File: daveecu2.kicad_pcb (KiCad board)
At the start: 4 copper layers, 160 x 117.5 mm, 242 parts, among them J1 CONN_BLACK, J2 CONN_GREY, J3 SWD, J4 USB_B, J5 USB_EXT, J6 Micro_SD_Card_Det, J7 HC-05, Q1 AO3401A, Q2 2N7002, Q3 2N7002, Q4 2N7002, U1 MPXH6250A, U10 USBLC6-2SC6, U11 MCP2551-I-SN, U12 STM32F429ZGTx, U13 VNLD5090, U14 VNLD5090, U16 ATECC608A-SSHDA, U2 VNLD5090, U3 VNLD5090, U4 TC4424A, U5 TC4424A, U6 SP720, U7 VNLD5090, U8 TPS5430DDA, U9 TPS5430DDA, Y1 25mhz, Y2 Crystal

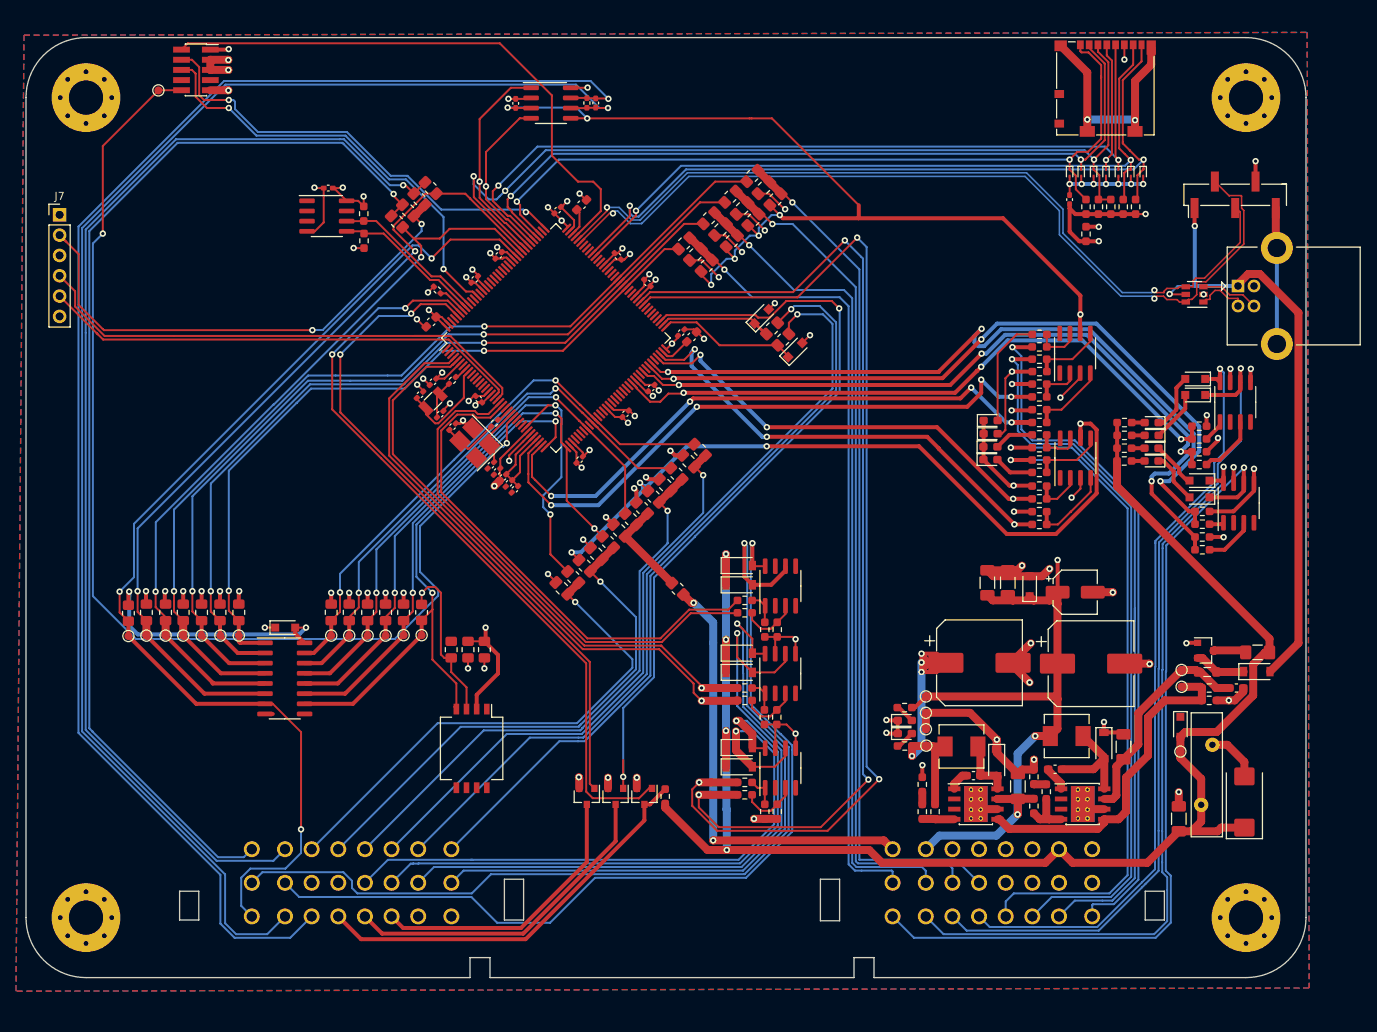
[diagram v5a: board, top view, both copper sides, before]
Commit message: Schematic and Layout Updates
* cleanup unused pins for DRC
* swap swd connector for the fancy one the phill uses
* swap out the CAN transciever for one more suitable for 3v3
* reroute CAN differential pair
* clean up copper pours
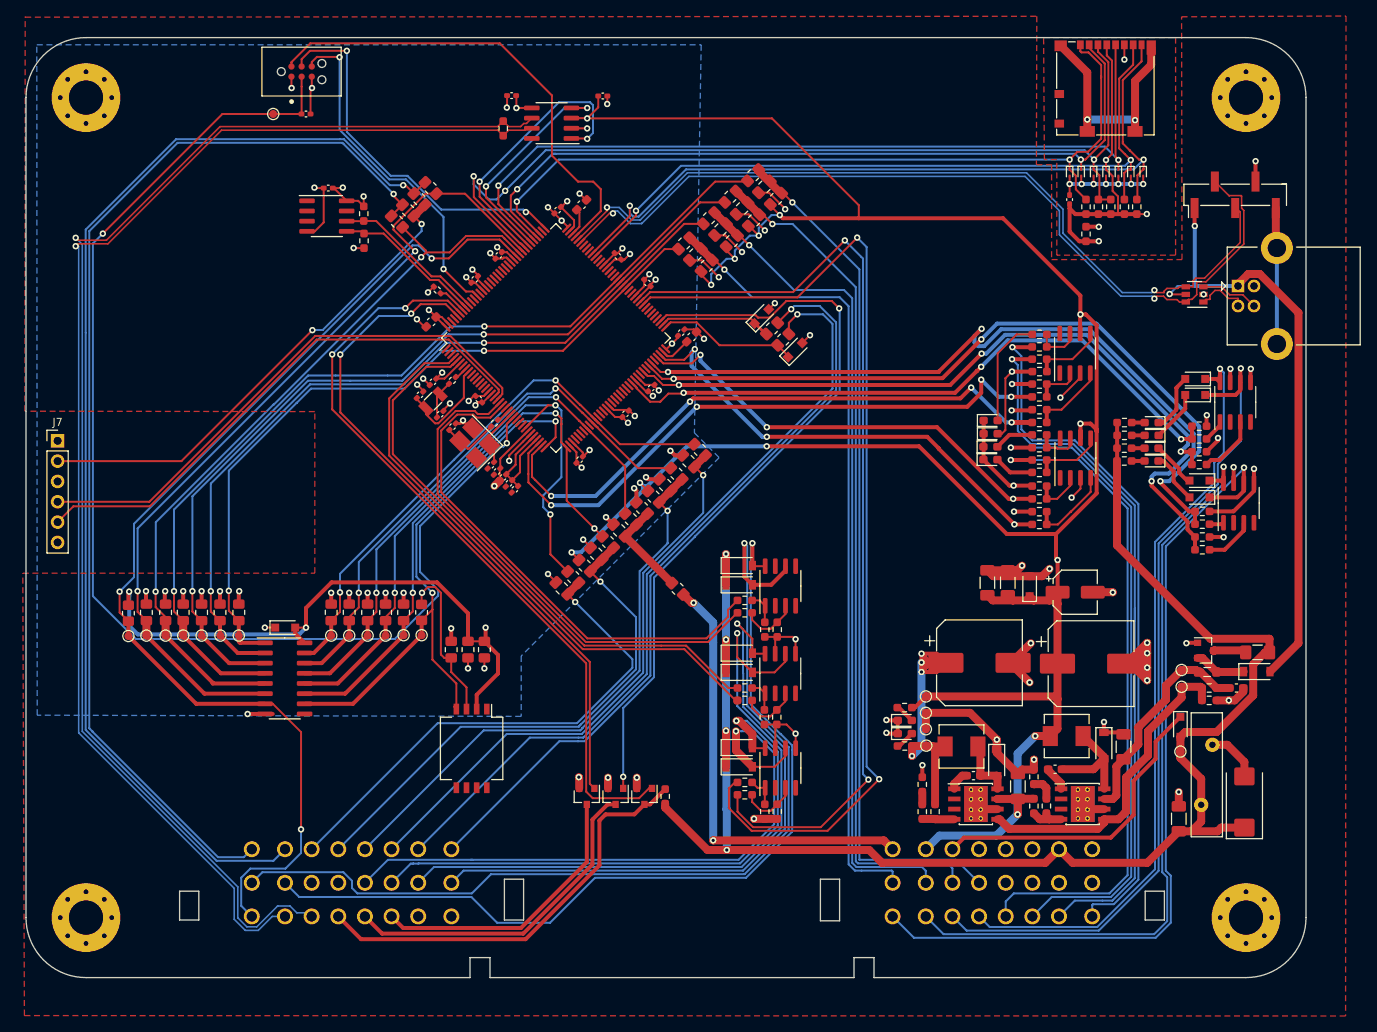
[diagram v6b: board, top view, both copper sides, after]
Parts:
- added C61: 100n, Capacitor_SMD:C_0402_1005Metric_Pad0.74x0.62mm_HandSolder, F.Cu at (87.1, 29.8)
- C23: value 0.1u -> 100n
- C24: value 100p -> 100n
- J3: footprint Connector_PinSocket_1.27mm:PinSocket_2x05_P1.27mm_Vertical_SMD -> TC2030-IDC-NL:TAG_TC2030-IDC-NL
- R58: value 60 -> 120; footprint Resistor_SMD:R_0402_1005Metric_Pad0.72x0.64mm_HandSolder -> Resistor_SMD:R_0603_1608Metric_Pad0.98x0.95mm_HandSolder
- U11: value MCP2551-I-SN -> TJA1051T-3
- moved J7 28.3 mm to (18.9, 72.9)
- moved C23 26.2 mm to (50.0, 32.0), turned to 0 degrees
- moved TP9 14.7 mm to (45.9, 32.0)
- moved J3 13.2 mm to (49.5, 26.8)
- moved R58 10.9 mm to (74.7, 33.9), turned to 270 degrees
- moved C24 10.6 mm to (75.7, 29.8), turned to 0 degrees
- moved U11 2.52 mm to (80.7, 33.2), turned to 180 degrees
- moved R56 1.80 mm to (142.6, 118.5)
- moved R76 0.15 mm to (152.3, 43.6)
- moved R77 0.15 mm to (153.8, 43.6)
- moved R10 0.14 mm to (105.9, 39.7)
- moved C46 0.14 mm to (107.3, 41.1)
- moved R2 0.11 mm to (106.0, 45.4)
- moved R4 0.10 mm to (108.8, 42.6)
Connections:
- C23 pad 1: VPROT -> NRST
- C24 pad 1: CANH -> GND
- C24 pad 2: CANL -> +3V3
- D35 pad 1: (no net) -> VREG
- J1 pad A1: (no net) -> GND
- J1 pad A6: GND -> VREG
- J2 pad C6: CANH -> CAN-
- J2 pad C7: CANL -> CAN+
- J3 pad 3: GND -> NRST
- R58 pad 1: CANL -> CAN-
- R58 pad 2: CANH -> CAN+
- U11 pad 5: VPROT -> +3V3
- U11 pad 6: CANL -> CAN-
- U11 pad 7: CANH -> CAN+
- U11 pad 8: GND -> (no net)
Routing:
- net CANH: track 187.2 -> 0.00 mm, vias 1 -> 0
- net CANL: track 182.4 -> 0.00 mm, vias 1 -> 0
- net CAN-: track 0.00 -> 168.7 mm, vias 0 -> 1
- net CAN+: track 0.00 -> 163.9 mm, vias 0 -> 1
- net VREG: track 0.00 -> 39.1 mm
- net VPROT: track 419.6 -> 455.0 mm, vias 19 -> 18
- net GND: track 290.5 -> 306.5 mm, vias 93 -> 97
- net SWDIO: track 71.9 -> 59.4 mm
- net NRST: track 145.7 -> 157.7 mm
- net SWO: track 54.2 -> 43.0 mm
- net SWCLK: track 56.8 -> 46.9 mm
- net /mcu/MCU-PWM1: track 128.5 -> 119.1 mm, vias 3 -> 2
- net MCU-CAN-TX: track 26.4 -> 35.4 mm, vias 1 -> 2
- net /mcu/MCU-VVT: track 134.5 -> 125.6 mm, vias 3 -> 2
- net UART7_RX: track 61.1 -> 68.3 mm
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- added copper zone on In2.Cu, net GND
- added copper zone on F.Cu, net SDIO_VDD
- added copper zone on B.Cu, net VPROT
- removed copper zone on B.Cu, net GND
- removed copper zone on In1.Cu, net GND
- removed copper zone on In1.Cu, net SDIO_VDD
- removed copper zone on In1.Cu, net VPROT

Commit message: More routing updates
* added stitching vias
* organized sensor sheet
* moved the CAN and Security chips closer together to clean up fills
* added silkscreen text to some things
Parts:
- added C62: 0.1uf, Capacitor_SMD:C_0805_2012Metric_Pad1.18x1.45mm_HandSolder, F.Cu at (78.0, 100.7)
- added C63: 1uf, Capacitor_SMD:C_0805_2012Metric_Pad1.18x1.45mm_HandSolder, F.Cu at (80.0, 100.7)
- added C64: 470pf, Capacitor_SMD:C_0805_2012Metric_Pad1.18x1.45mm_HandSolder, F.Cu at (75.9, 100.7)
- added R89: 470, Resistor_SMD:R_0805_2012Metric_Pad1.20x1.40mm_HandSolder, F.Cu at (66.7, 94.3)
- added TP1: TP_BARO, TestPoint:TestPoint_Pad_D1.0mm, F.Cu at (66.7, 97.2)
- added U15: MPXH6250A, Sensor_Pressure:Freescale_98ARH99066A, F.Cu at (79.3, 111.3)
- moved C61 36.0 mm to (56.5, 48.9)
- moved C24 35.1 mm to (45.5, 47.6)
- moved R58 34.4 mm to (44.4, 50.1)
- moved U11 34.4 mm to (50.4, 49.5)
- moved R50 14.5 mm to (45.9, 38.9), turned to 90 degrees
- moved R51 11.5 mm to (46.0, 42.3), turned to 270 degrees
- moved C54 9.22 mm to (43.9, 43.8), turned to 270 degrees
- moved TP9 3.98 mm to (49.4, 34.0)
- moved U16 3.46 mm to (50.6, 42.0), turned to 180 degrees
- moved C45 2.26 mm to (71.8, 100.7)
- moved C47 2.26 mm to (69.7, 100.7)
- moved C9 2.26 mm to (73.8, 100.7)
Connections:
- U6 pad 9: (no net) -> ADC-CLAMP-8
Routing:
- net VPROT: track 455.0 -> 414.5 mm, vias 18 -> 21
- net ADC-CLAMP-8: track 0.00 -> 40.0 mm, vias 0 -> 2
- net CAN-: track 168.7 -> 135.5 mm
- net CAN+: track 163.9 -> 130.7 mm
- net Net-(C64-Pad2): track 0.00 -> 23.8 mm, vias 0 -> 2
- net I2C1_SDA: track 19.6 -> 39.3 mm, vias 0 -> 2
- net I2C1_SDL: track 19.6 -> 36.2 mm, vias 0 -> 2
- net MCU-CAN-RX: track 28.0 -> 36.8 mm, vias 2 -> 1
- net ADC-CLAMP-9: track 74.1 -> 81.4 mm, vias 2 -> 3
- net MCU-CAN-TX: track 35.4 -> 41.7 mm, vias 2 -> 3
- net SWDIO: track 59.4 -> 55.9 mm, vias 0 -> 2
- net NRST: track 157.7 -> 155.1 mm, vias 2 -> 4
- net Net-(C47-Pad2): track 20.8 -> 18.4 mm, vias 1 -> 2
- net +3V3: track 111.8 -> 109.9 mm, vias 25 -> 24
- net GND: track 306.5 -> 306.9 mm, vias 97 -> 101
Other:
- net class Default: clearance 0.2 -> 0.1999
- rule trace_clearance: 0.2 -> 0.1999
- board text added: "+3.3V"
- board text added: "+5V"
- board text added: "BLACK"
- board text added: "GRAY"
- board text added: "HC-05"
- board text added: "IGN 1 IGN 2 IGN 3 IGN 4"
- board text added: "INJ 1 INJ 2 INJ 3 INJ 4"
- board text added: "SWD"
- board text added: "USB-EXT"
- board text added: "daveecu2 speeduino mainboard connor rigby © 2021"
- board text added: "revision 1 2021-05-07"
